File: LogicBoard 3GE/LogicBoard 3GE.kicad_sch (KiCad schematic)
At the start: 165 parts, among them IC201 2363, IC202 74LS00, IC203 74LS32, IC204 2114, IC205 2114, IC206 68A09, IC207 6522, IC208 AY3-8912, IC301 MC1408, IC302 CD4052B, IC303 LF347, IC304 LF353, IC305 4066, J201 CART, J202 DB9_Male, J203 DB9_Male, J204 Power, J301 Video, J302 Audio, Q301 2N3905, Q302 2N3905, Q303 2N3904, SW201 Reset, Y201 6MHz

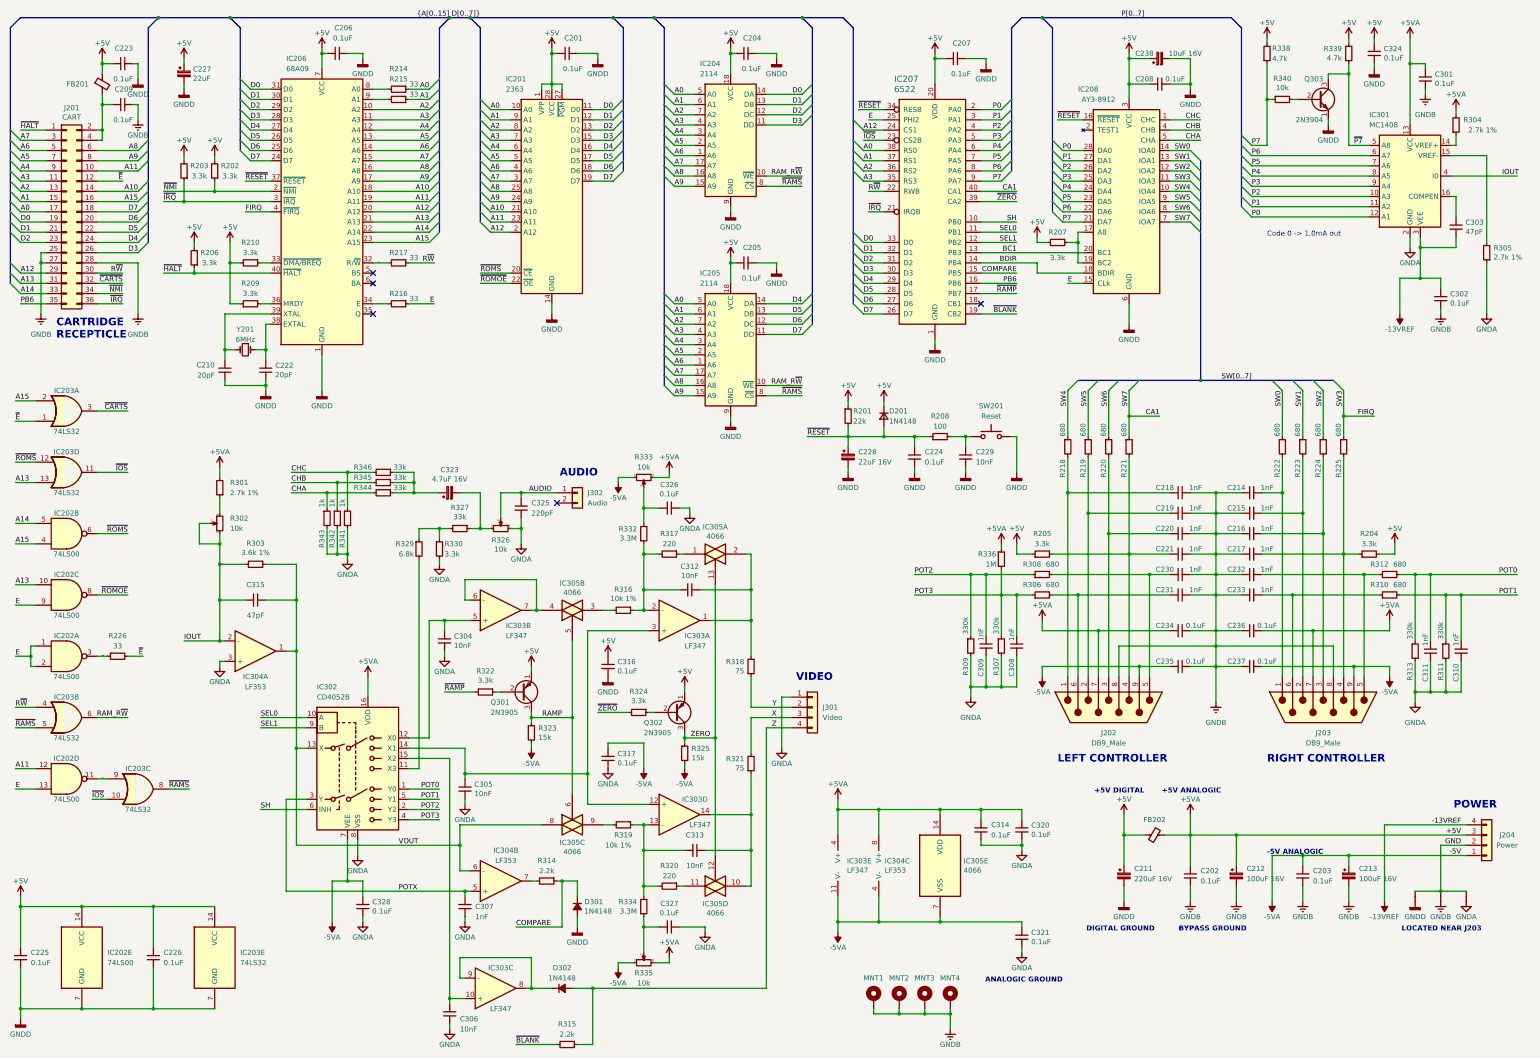
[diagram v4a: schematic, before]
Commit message: correction to the LM379 on the PowerBoard
- Convert to Kicad 8
- Correction to the LM379 on the PowerBoard and C405,C406,R404,R411
- Correct value of F101
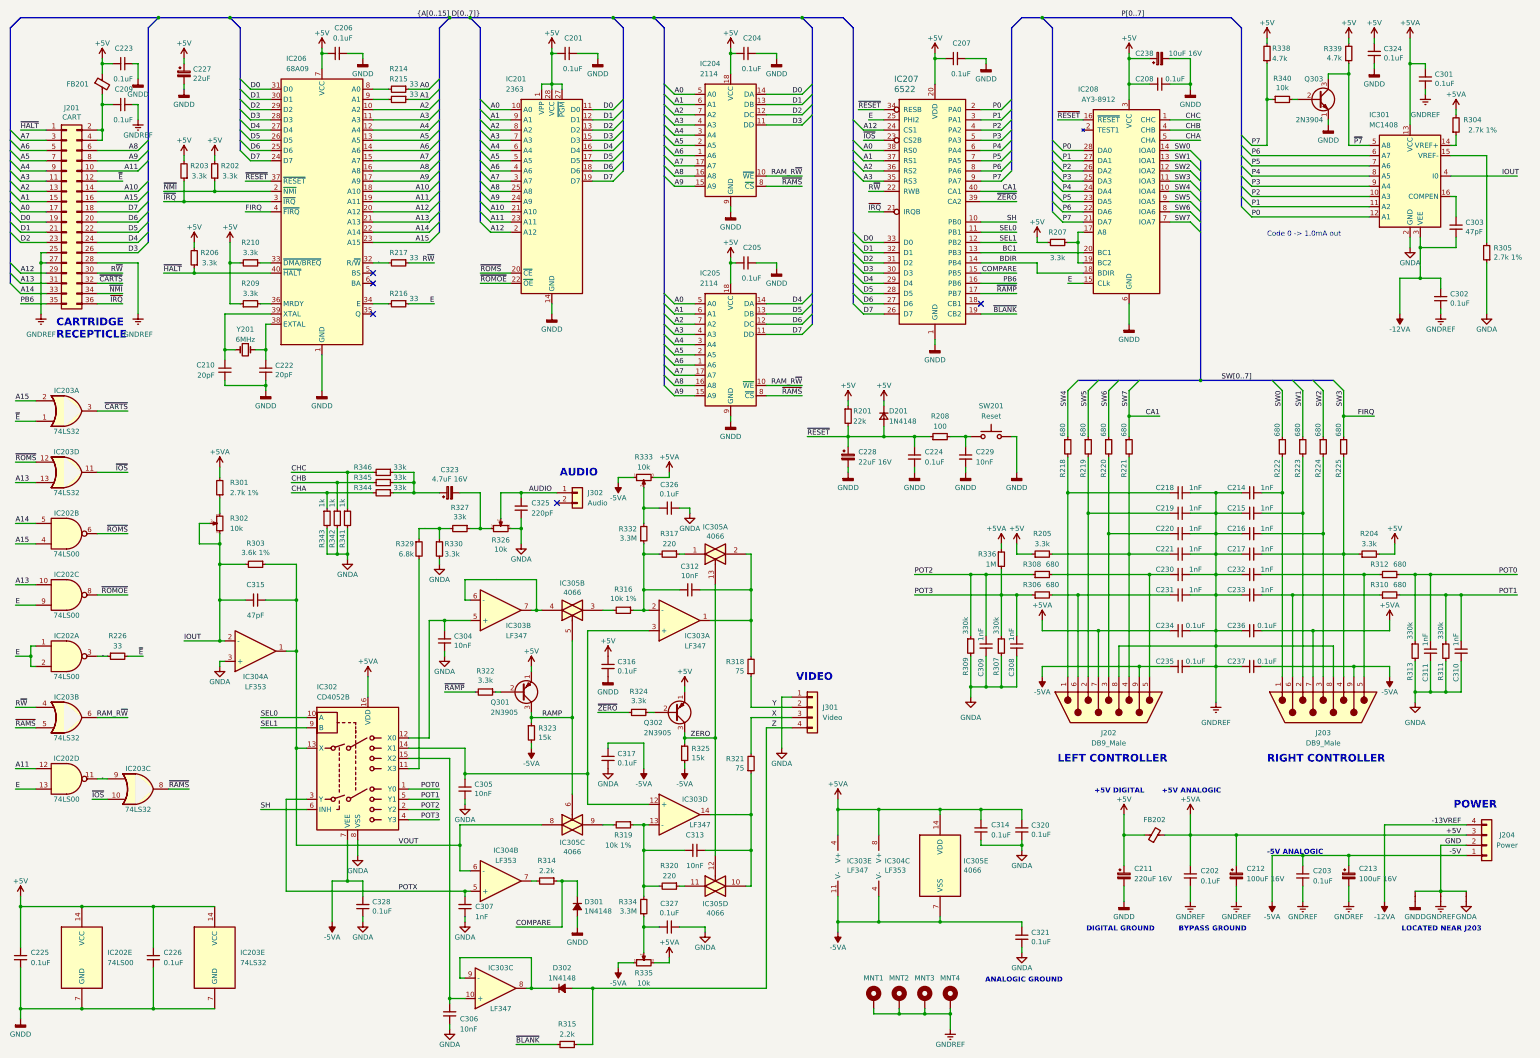
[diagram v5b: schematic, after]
